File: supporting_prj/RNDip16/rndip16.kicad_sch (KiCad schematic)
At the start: 25 parts, among them J1 Conn_01x16_Pin, J2 Conn_01x16_Pin

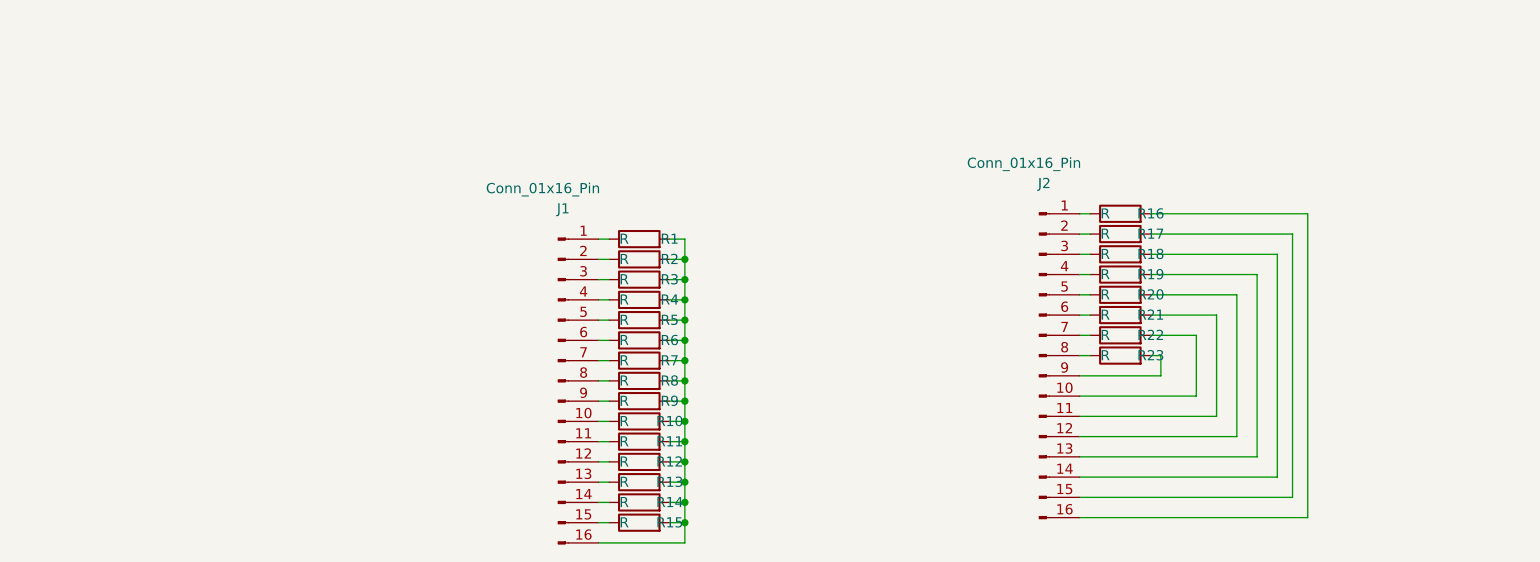
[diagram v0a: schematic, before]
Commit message: RNDip fix
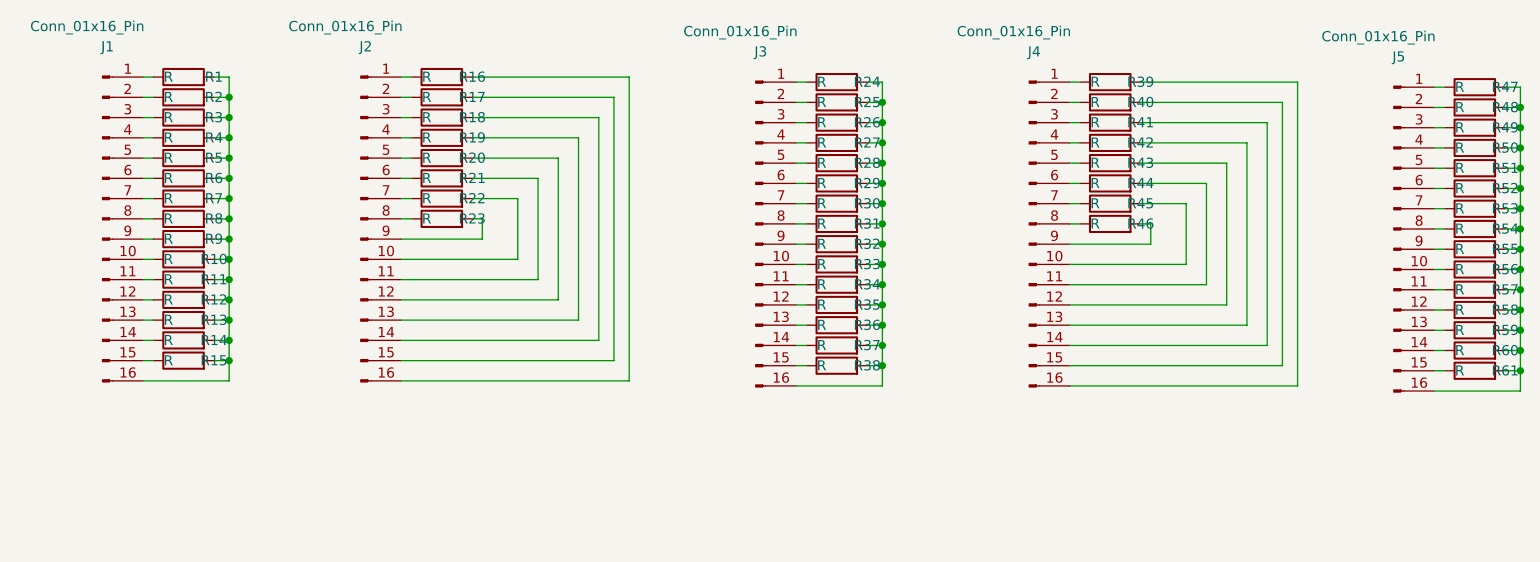
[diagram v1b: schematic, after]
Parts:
- added J3, J4, J5: Conn_01x16_Pin, RNDip16:Dip16_package, symbol Connector:Conn_01x16_Pin
- added R24, R25, R26, R27, R28, R29, R30, R31, R32, R33, R34, R35, R36, R37, R38, R39, R40, R41, R42, R43, R44, R45, R46, R47, R48, R49, R50, R51, R52, R53, R54, R55, R56, R57, R58, R59, R60, R61: R, RNDip16:R_0805, symbol Device:R
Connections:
- new net: J4.6 (Pin_6), R44.1
- new net: J4.11 (Pin_11), R44.2
- new net: J5.7 (Pin_7), R53.1
- new net: J5.16 (Pin_16), R47.2, R48.2, R49.2, R50.2, R51.2, R52.2, R53.2, R54.2, R55.2, R56.2, R57.2, R58.2, R59.2, R60.2, R61.2
- new net: J5.12 (Pin_12), R58.1
- new net: J3.15 (Pin_15), R38.1
- new net: J3.16 (Pin_16), R24.2, R25.2, R26.2, R27.2, R28.2, R29.2, R30.2, R31.2, R32.2, R33.2, R34.2, R35.2, R36.2, R37.2, R38.2
- new net: J5.1 (Pin_1), R47.1
- new net: J3.11 (Pin_11), R34.1
- new net: J5.10 (Pin_10), R56.1
- new net: J5.11 (Pin_11), R57.1
- new net: J5.13 (Pin_13), R59.1
- new net: J5.14 (Pin_14), R60.1
- new net: J5.15 (Pin_15), R61.1
- new net: J5.2 (Pin_2), R48.1
- new net: J5.3 (Pin_3), R49.1
- new net: J5.4 (Pin_4), R50.1
- new net: J5.5 (Pin_5), R51.1
- new net: J5.6 (Pin_6), R52.1
- new net: J5.8 (Pin_8), R54.1
- new net: J5.9 (Pin_9), R55.1
- new net: J3.6 (Pin_6), R29.1
- new net: J3.2 (Pin_2), R25.1
- new net: J3.1 (Pin_1), R24.1
- new net: J3.10 (Pin_10), R33.1
- new net: J3.12 (Pin_12), R35.1
- new net: J3.13 (Pin_13), R36.1
- new net: J3.14 (Pin_14), R37.1
- new net: J3.3 (Pin_3), R26.1
- new net: J3.4 (Pin_4), R27.1
- new net: J3.5 (Pin_5), R28.1
- new net: J3.7 (Pin_7), R30.1
- new net: J3.8 (Pin_8), R31.1
- new net: J3.9 (Pin_9), R32.1
- new net: J4.2 (Pin_2), R40.1
- new net: J4.15 (Pin_15), R40.2
- new net: J4.4 (Pin_4), R42.1
- new net: J4.13 (Pin_13), R42.2
- new net: J4.1 (Pin_1), R39.1
- new net: J4.16 (Pin_16), R39.2
- new net: J4.8 (Pin_8), R46.1
- new net: J4.9 (Pin_9), R46.2
- new net: J4.5 (Pin_5), R43.1
- new net: J4.12 (Pin_12), R43.2
- new net: J4.7 (Pin_7), R45.1
- new net: J4.10 (Pin_10), R45.2
- new net: J4.3 (Pin_3), R41.1
- new net: J4.14 (Pin_14), R41.2
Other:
- moved on the sheet: J1, J2, R1, R10, R11, R12, R13, R14, R15, R16, R17, R18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
